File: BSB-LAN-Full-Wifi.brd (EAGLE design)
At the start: 86.5 x 32.8 mm, 72 parts, among them IC4 SY8089AAAC, IC6 CH340X, Q1 BC847, Q2 BC857, Q5 BC847, Q6 BC847, Q7 WPM2015-3/TR, U2 ESDS314DBV

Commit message: Reduce Wifi BoM Complexity
There were some weird values left that were holdovers from the LAN board where they were used elsewhere.
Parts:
- C18: value 220uF 25V -> 100uF 20V
- C20, C21: value 1nF 3kV -> 1nF 2kV; device BSB-LAN:C1808 -> BSB-LAN:C1206L
- D6: value SS510B -> SS34; device BSB-LAN:SMB -> BSB-LAN:SMA
- R40, R43: value 180k 1% -> 200k 1%
- R41: value 12.1k 1% -> 22k 1%
- R42: value 28.7k 1% -> 22k 1%
- moved C20 1.05 mm to (28.4, 11.3)
- moved C21 0.41 mm to (28.4, 8.90)
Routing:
- net SUP-GND: track 27.2 -> 27.8 mm
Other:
- board text added: "1.5kV Max"

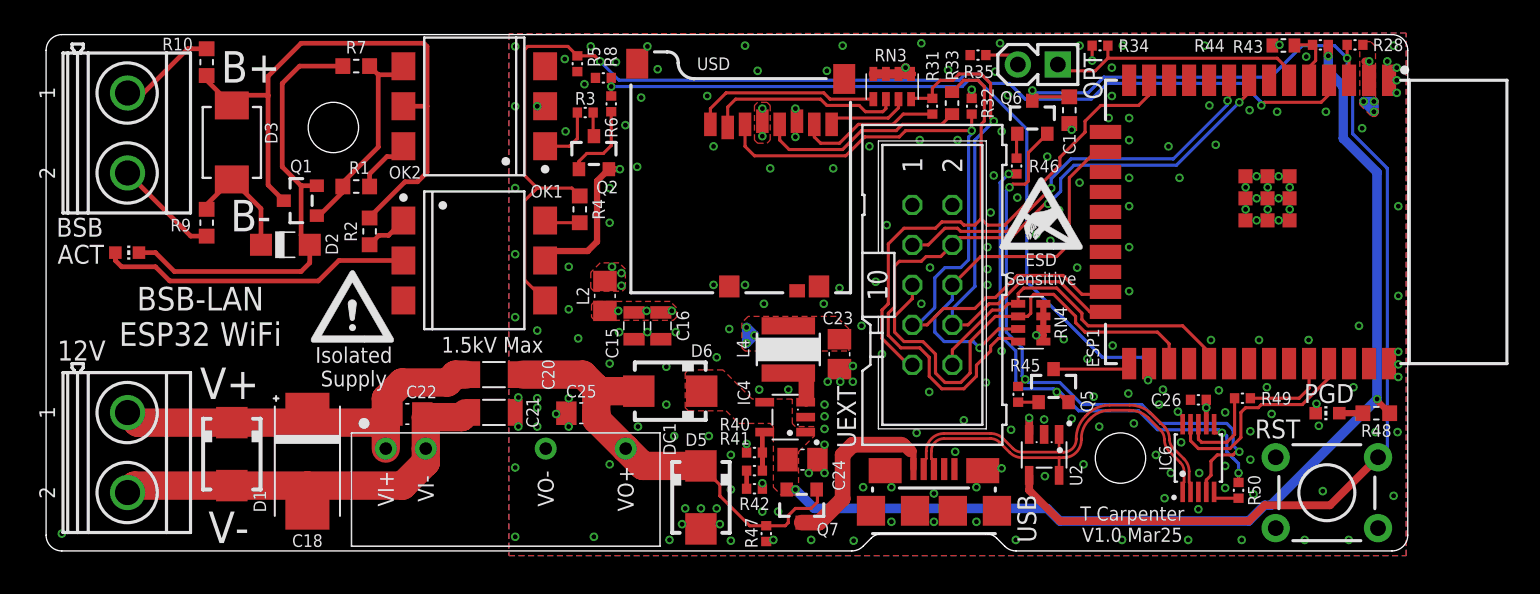
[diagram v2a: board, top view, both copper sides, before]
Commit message: Correct ESP32 Prog Control + Update Libraries
1. Correct the control of automatic bootloader entry by adding missing resistor from GPIO2 to GPIO0.
2. Update libraries and fix layout to account for changes.
3. Change the LAN versions of the boards to use the ESP32 with external antenna. If the PCB antenna is used then it is not possible to get the PCB into the enclosure because components stick out on both ends!
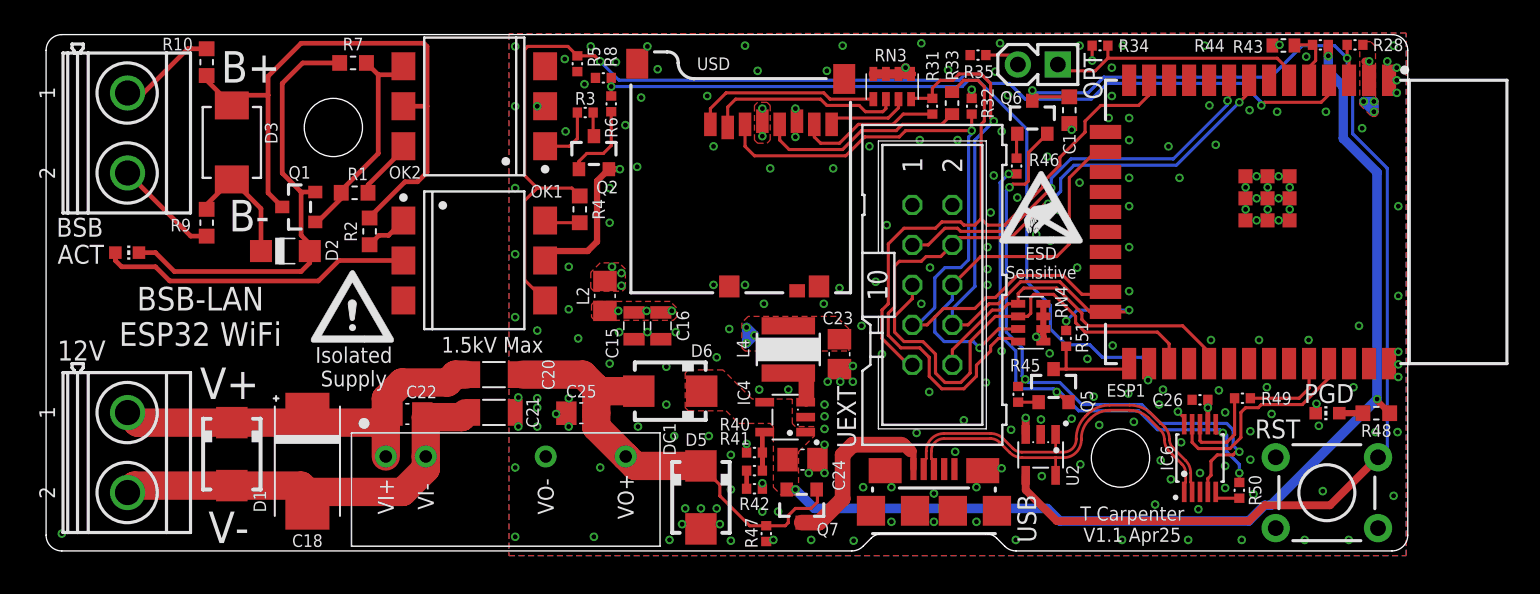
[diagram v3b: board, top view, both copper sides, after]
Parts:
- added R51: 220R, BSB-LAN:R0402
- moved Q1 0.41 mm to (16.1, 21.9)
- moved R1 0.41 mm to (19.6, 22.9)
- moved D2 0.40 mm to (15.2, 19.1)
- moved U$2 0.40 mm to (63.2, 21.4)
- moved R7 0.28 mm to (19.5, 31.1)
- moved U2 0.22 mm to (63.2, 6.20)
- moved C26 0.10 mm to (73.3, 9.70)
- moved IC6 0.10 mm to (73.3, 6.00)
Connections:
- net ESP-GPIO0: now also R51.1
- net ESP-SD-DATA: now also R51.2
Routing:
- net ESP-SD-DATA: track 34.6 -> 41.0 mm, vias 1 -> 3
- net ESP-GPIO0: track 5.25 -> 6.70 mm
- net BSB-TXD: track 50.7 -> 51.6 mm
- net BSB-TX-E: track 13.6 -> 14.3 mm
- net SUP-12V0: track 27.1 -> 27.6 mm
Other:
- board text added: "T Carpenter V1.1 Apr25"
- board text removed: "T Carpenter V1.0 Mar25"

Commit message: Adjust Silkscreen
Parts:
- moved U$3 15.0 mm to (11.2, 29.4), turned to 0 degrees
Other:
- board text added: "BSB to WiFi ESP32 Based"
- board text added: "github://TCWORLD/BSB-Interface-PCBs"
- board text removed: "BSB-LAN ESP32 WiFi"
- board text removed: "github://TCWORLD/BSB-LAN-CircuitBoard github://fredlcore/BSB-LAN github://OLIMEX/ESP32-POE-ISO"
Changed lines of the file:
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@@
 <text x="13" y="30.85" size="2" layer="21" font="vector" ratio="15" align="center">B+</text>
 <text x="12.9" y="21.4" size="2" layer="21" font="vector" ratio="15" rot="R180" align="center">B-</text>
-<text x="9.8" y="15" size="1.5" layer="21" font="vector" ratio="15" rot="R180" align="center">BSB-LAN
-ESP32 WiFi
+<text x="8.6" y="14.6" size="1.5" layer="21" font="vector" ratio="15" rot="R180" align="center">BSB to WiFi
+ESP32 Based
 </text>
 <text x="69" y="1.8" size="0.9" layer="21" font="vector" ratio="15" rot="R180" align="center">T Carpenter
@@
 Supply</text>
 <text x="1.6" y="27.15" size="1" layer="22" font="vector" ratio="15" rot="MR90" align="center">JLCJLCJLC</text>
-<text x="22.8" y="29.2" size="0.8" layer="22" font="vector" ratio="15" rot="MR90" align="center">Open
+<text x="11" y="26" size="0.8" layer="22" font="vector" ratio="15" rot="MR0" align="center">Open
 Hardware</text>
-<text x="10.25" y="32.6" size="1" layer="22" font="vector" ratio="15" rot="MR270" align="center-left">github://TCWORLD/BSB-LAN-CircuitBoard
-github://fredlcore/BSB-LAN
-github://OLIMEX/ESP32-POE-ISO</text>
-<text x="15.6" y="0.8" size="1" layer="22" font="vector" ratio="15" rot="MR90" align="center-left">Based on:
+<text x="2.4" y="1.25" size="1" layer="22" font="vector" ratio="15" rot="MR180" align="center-left">github://TCWORLD/BSB-Interface-PCBs</text>
+<text x="28.8" y="22.6" size="1" layer="22" font="vector" ratio="15" rot="MR0" align="center-left">Based on:
 Olimex ESP32-POE-ISO
 Fredlcore BSB-LAN</text>
@@
 </element>
 <element name="BSB" library="BSB-LAN" package="MKDSN1_5-2-5_08" value="MKDSN1,5/2-5,08" x="5.15" y="26.65" smashed="yes" rot="R270">
-<attribute name="NAME" x="2.14" y="20.66" size="1.2" layer="25" font="vector" ratio="15" align="center"/>
+<attribute name="NAME" x="1.94" y="20.66" size="1.2" layer="25" font="vector" ratio="15" align="center"/>
 <attribute name="LCSC_PART" value="C5183989" x="5.15" y="26.65" size="1.778" layer="27" rot="R270" display="off"/>
 </element>
@@
 <element name="ACT" library="BSB-LAN" package="CHIP-LED0603" value="red" x="5.15" y="19.05" smashed="yes" rot="R270">
 <attribute name="LCSC_PART" value="C2286" x="-34.22" y="-1.27" size="1.778" layer="27" rot="R270" display="off"/>
-<attribute name="NAME" x="2.2" y="18.945" size="1.2" layer="25" font="vector" ratio="15" rot="R180" align="center"/>
+<attribute name="NAME" x="2" y="19.145" size="1.2" layer="25" font="vector" ratio="15" rot="R180" align="center"/>
 <attribute name="JLC_ROT" value="270" x="5.15" y="19.05" size="1.778" layer="27" rot="R270" display="off"/>
 </element>
@@
 </element>
 <element name="R9" library="BSB-LAN" package="R0603" value="10R" x="10.2" y="20.95" smashed="yes" rot="R90">
-<attribute name="NAME" x="8.55" y="20.8" size="0.8" layer="25" font="vector" ratio="15" align="center"/>
+<attribute name="NAME" x="9" y="20.55" size="0.8" layer="25" font="vector" ratio="15" rot="R90" align="center"/>
 <attribute name="LCSC_PART" value="C22859" x="10.2" y="20.95" size="1.778" layer="27" rot="R90" display="off"/>
 </element>
 <element name="U$1" library="BSB-LAN" package="WARN-TINY" value="" x="19.45" y="15.1" smashed="yes"/>
 <element name="U$2" library="BSB-LAN" package="ESD-TINY" value="" x="63.2" y="21.4" smashed="yes"/>
-<element name="U$3" library="BSB-LAN" package="OSHW-LOGO-M" value="DNI" x="26.2" y="29.2" smashed="yes" rot="MR90">
-<attribute name="VALUE" value="DNI" x="26.2" y="29.2" size="1.778" layer="28" rot="MR90" display="off"/>
+<element name="U$3" library="BSB-LAN" package="OSHW-LOGO-M" value="DNI" x="11.2" y="29.4" smashed="yes" rot="MR0">
+<attribute name="VALUE" value="DNI" x="11.2" y="29.4" size="1.778" layer="28" rot="MR0" display="off"/>
 </element>
 <element name="DC1" library="BSB-LAN" package="SIP7-N" value="F1205S-2WR2SC" x="29.2" y="6.6" smashed="yes">
@@
 <element name="12V" library="BSB-LAN" package="MKDSN1_5-2-5_08" value="MKDSN1,5/2-5,08" x="5.15" y="6.35" smashed="yes" rot="R270">
 <attribute name="LCSC_PART" value="C5183989" x="21.15" y="21.15" size="1" layer="27" font="vector" ratio="15" rot="R270" display="off"/>
-<attribute name="NAME" x="2.25" y="12.83" size="1.27" layer="25" font="vector" ratio="15" align="center"/>
+<attribute name="NAME" x="2.05" y="12.63" size="1.27" layer="25" font="vector" ratio="15" align="center"/>
 <attribute name="VALUE" x="-2.47" y="6.35" size="1.27" layer="27" font="vector" ratio="15" rot="R270" align="center"/>
 </element>
